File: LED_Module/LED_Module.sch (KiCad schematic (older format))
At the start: 16 parts, among them P3 CONN_02X04, P4 CONN_02X04, U1 AL8805WS, U2 AL8805WS

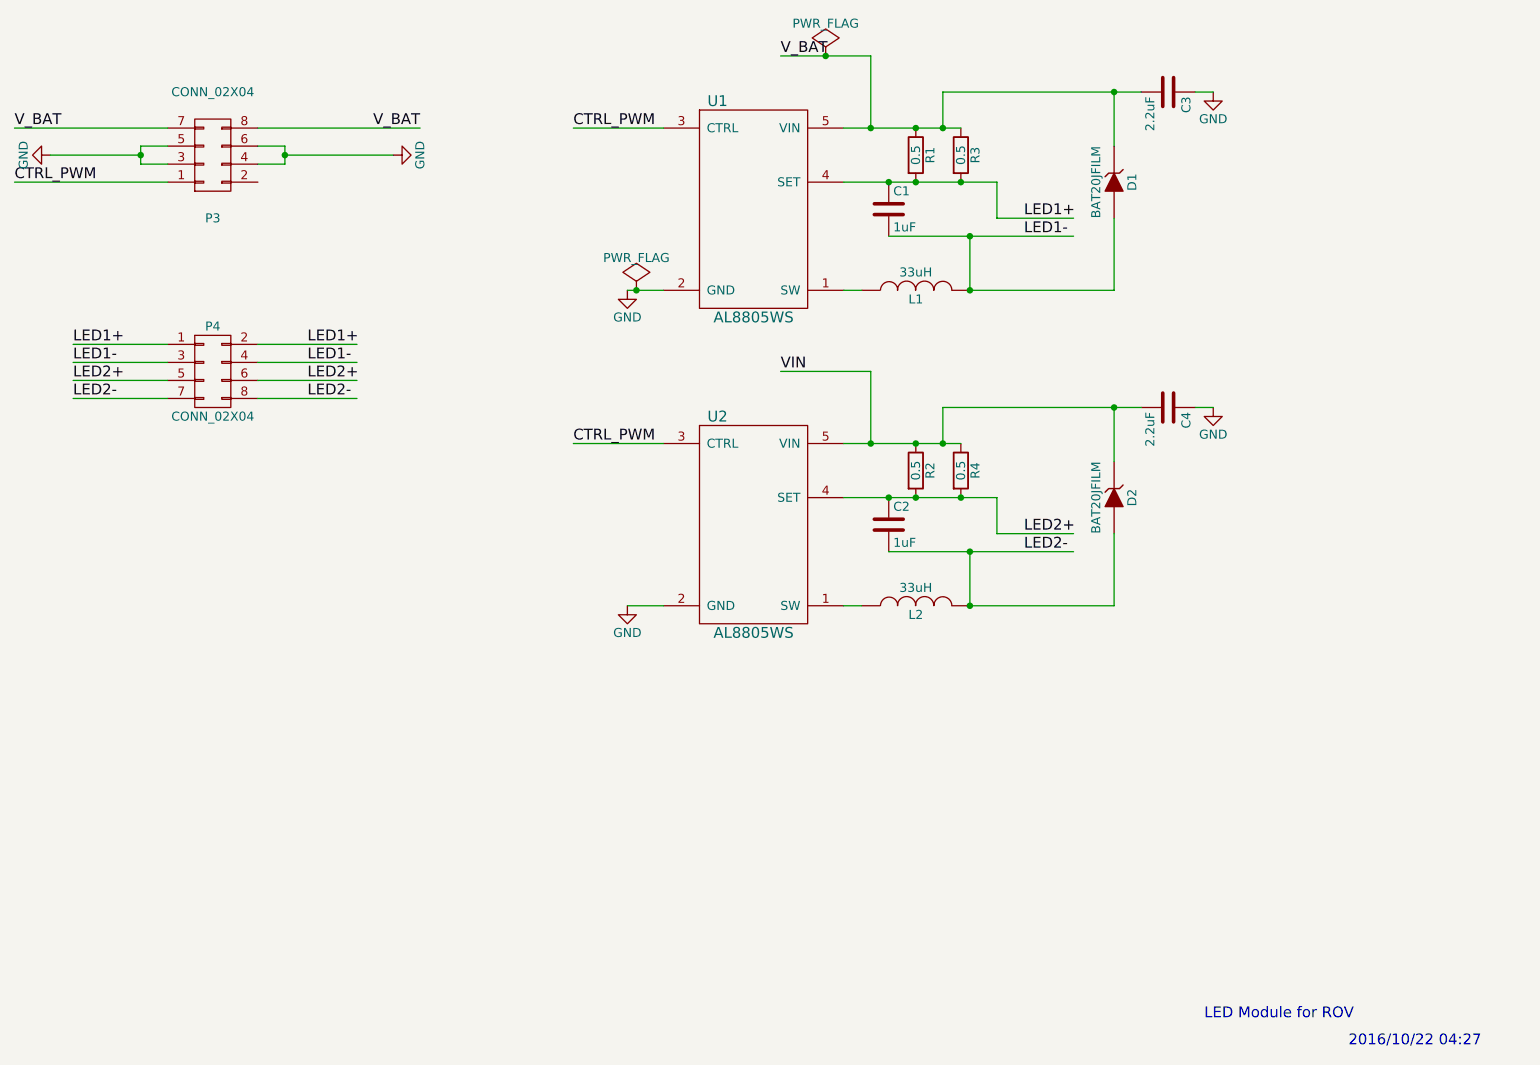
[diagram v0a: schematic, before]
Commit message: Recover LED_Module project
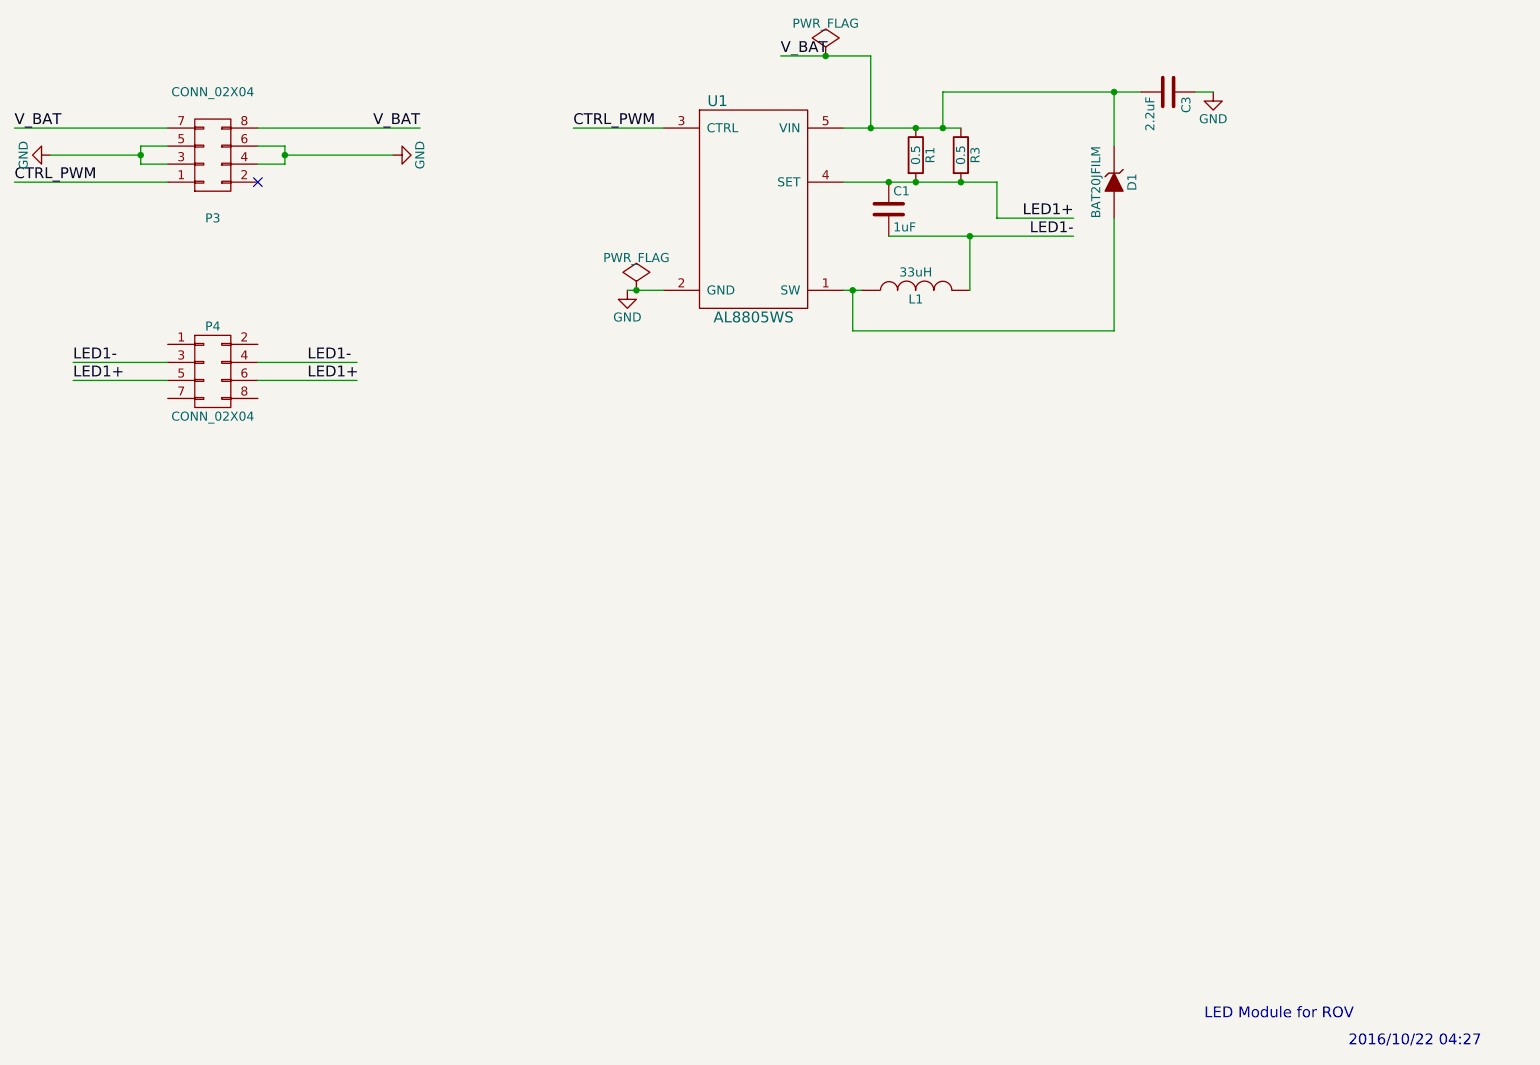
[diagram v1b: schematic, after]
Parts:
- removed C2: 1uF, Capacitors_SMD:C_0805_HandSoldering, symbol C
- removed C4: 2.2uF, Capacitors_SMD:C_0805_HandSoldering, symbol C
- removed D2: BAT20JFILM, w_smd_diode:sod323, symbol ZENER
- removed L2: 33uH, inductor:inductor_33uH, symbol INDUCTOR
- removed R2, R4: 0.5, Resistors_SMD:R_0805_HandSoldering, symbol R
- removed U2: AL8805WS, w_smd_trans:sot23-5, symbol AL8805WS
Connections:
- net labels removed: LED2+, LED2-, VIN
- wire segments 53 -> 33
- no-connect marks 0 -> 1
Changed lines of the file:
@@
 	1    0    0    -1
 $EndComp
-Wire Wire Line
-	5350 3450 5450 3450
-Wire Wire Line
-	5600 3150 6625 3150
-Wire Wire Line
-	6200 2850 6200 3050
-Connection ~ 5600 2850
 $Comp
 L R R1
@@
 	1    0    0    -1
 $EndComp
-Connection ~ 5750 2850
-Connection ~ 5750 2550
-Wire Wire Line
-	6050 3450 6050 3150
-Connection ~ 6050 3150
-Wire Wire Line
-	6050 3450 6850 3450
-Wire Wire Line
-	6850 3450 6850 3050
-Wire Wire Line
-	5900 2550 5900 2350
-Wire Wire Line
-	5900 2350 7000 2350
-Wire Wire Line
-	6850 2350 6850 2650
-Connection ~ 5900 2550
-Connection ~ 6850 2350
 $Comp
 L C C3
@@
 	1    0    0    -1
 $EndComp
-Wire Wire Line
-	7400 2350 7300 2350
-Wire Wire Line
-	5500 2150 5500 2550
-Wire Wire Line
-	5000 2150 5500 2150
-Connection ~ 5500 2550
-Wire Wire Line
-	3850 2550 4350 2550
 Text Label 3850 2550 0    60   ~ 0
 CTRL_PWM
@@
 V_BAT
 $Comp
-L AL8805WS U2
-U 1 1 580AA03A
-P 4850 4750
-F 0 "U2" H 4650 5350 60  0000 C CNN
-F 1 "AL8805WS" H 4850 4150 60  0000 C CNN
-F 2 "w_smd_trans:sot23-5" H 4850 4750 60  0001 C CNN
-F 3 "" H 4850 4750 60  0001 C CNN
-	1    4850 4750
-	1    0    0    -1
-$EndComp
-$Comp
-L INDUCTOR L2
-U 1 1 580AA040
-P 5750 5200
-F 0 "L2" V 5700 5200 50  0000 C CNN
-F 1 "33uH" V 5850 5200 50  0000 C CNN
-F 2 "inductor:inductor_33uH" H 5750 5200 50  0001 C CNN
-F 3 "" H 5750 5200 50  0000 C CNN
-	1    5750 5200
-	0    -1   -1   0
-$EndComp
-$Comp
-L GND #PWR03
-U 1 1 580AA058
-P 4150 5200
-F 0 "#PWR03" H 4150 4950 50  0001 C CNN
-F 1 "GND" H 4150 5050 50  0000 C CNN
-F 2 "" H 4150 5200 50  0000 C CNN
-F 3 "" H 4150 5200 50  0000 C CNN
-	1    4150 5200
-	1    0    0    -1
-$EndComp
-Wire Wire Line
-	4150 5200 4350 5200
-Wire Wire Line
-	5350 5200 5450 5200
-Wire Wire Line
-	5600 4900 6625 4900
-Wire Wire Line
-	6200 4600 6200 4800
-Wire Wire Line
-	6050 5200 6050 4900
-Connection ~ 6050 4900
-Wire Wire Line
-	6050 5200 6850 5200
-Wire Wire Line
-	6850 5200 6850 4800
-Wire Wire Line
-	5900 4300 5900 4100
-Wire Wire Line
-	5900 4100 7000 4100
-Wire Wire Line
-	6850 4100 6850 4400
-Connection ~ 5900 4300
-Connection ~ 6850 4100
-$Comp
-L C C4
-U 1 1 580AA079
-P 7150 4100
-F 0 "C4" H 7175 4200 50  0000 L CNN
-F 1 "2.2uF" H 7175 4000 50  0000 L CNN
-F 2 "Capacitors_SMD:C_0805_HandSoldering" H 7188 3950 50  0001 C CNN
-F 3 "" H 7150 4100 50  0000 C CNN
-	1    7150 4100
-	0    1    1    0
-$EndComp
-$Comp
-L GND #PWR04
-U 1 1 580AA07F
-P 7400 4100
-F 0 "#PWR04" H 7400 3850 50  0001 C CNN
-F 1 "GND" H 7400 3950 50  0000 C CNN
-F 2 "" H 7400 4100 50  0000 C CNN
-F 3 "" H 7400 4100 50  0000 C CNN
-	1    7400 4100
-	1    0    0    -1
-$EndComp
-Wire Wire Line
-	7400 4100 7300 4100
-Wire Wire Line
-	5500 4300 5500 3900
-Wire Wire Line
-	5500 3900 5000 3900
-Connection ~ 5500 4300
-Wire Wire Line
-	3850 4300 4350 4300
-Text Label 3850 4300 0    60   ~ 0
-CTRL_PWM
-Text Label 5000 3900 0    60   ~ 0
-VIN
-$Comp
-L PWR_FLAG #FLG05
+L PWR_FLAG #FLG03
 U 1 1 580AA3E5
 P 5250 2150
-F 0 "#FLG05" H 5250 2245 50  0001 C CNN
+F 0 "#FLG03" H 5250 2245 50  0001 C CNN
 F 1 "PWR_FLAG" H 5250 2330 50  0000 C CNN
 F 2 "" H 5250 2150 50  0000 C CNN
@@
 	1    0    0    -1
 $EndComp
-Connection ~ 5250 2150
-Wire Wire Line
-	4150 3450 4350 3450
-$Comp
-L PWR_FLAG #FLG06
+$Comp
+L PWR_FLAG #FLG04
 U 1 1 580AAE48
 P 4200 3450
-F 0 "#FLG06" H 4200 3545 50  0001 C CNN
+F 0 "#FLG04" H 4200 3545 50  0001 C CNN
 F 1 "PWR_FLAG" H 4200 3630 50  0000 C CNN
 F 2 "" H 4200 3450 50  0000 C CNN
@@
 	1    0    0    -1
 $EndComp
-Connection ~ 4200 3450
 Text Notes 7350 7500 0    60   ~ 0
 LED Module for ROV
@@
 	1    0    0    -1
 $EndComp
-Connection ~ 6000 2850
-$Comp
-L ZENER D2
-U 1 1 580C265A
-P 6850 4600
-F 0 "D2" H 6850 4700 50  0000 C CNN
-F 1 "BAT20JFILM" H 6850 4500 50  0000 C CNN
-F 2 "w_smd_diode:sod323" H 6850 4600 50  0001 C CNN
-F 3 "" H 6850 4600 50  0000 C CNN
-	1    6850 4600
-	0    1    1    0
-$EndComp
-Wire Wire Line
-	5350 4600 6200 4600
-Wire Wire Line
-	6000 4300 5350 4300
-Wire Wire Line
-	6200 2850 5350 2850
-Wire Wire Line
-	5350 2550 6000 2550
-$Comp
-L R R4
-U 1 1 580C75A6
-P 6000 4450
-F 0 "R4" V 6080 4450 50  0000 C CNN
-F 1 "0.5" V 6000 4450 50  0000 C CNN
-F 2 "Resistors_SMD:R_0805_HandSoldering" V 5930 4450 50  0001 C CNN
-F 3 "" H 6000 4450 50  0000 C CNN
-	1    6000 4450
-	1    0    0    -1
-$EndComp
-$Comp
-L R R2
-U 1 1 580C7673
-P 5750 4450
-F 0 "R2" V 5830 4450 50  0000 C CNN
-F 1 "0.5" V 5750 4450 50  0000 C CNN
-F 2 "Resistors_SMD:R_0805_HandSoldering" V 5680 4450 50  0001 C CNN
-F 3 "" H 5750 4450 50  0000 C CNN
-	1    5750 4450
-	1    0    0    -1
-$EndComp
-Connection ~ 6000 4600
-Connection ~ 5750 4600
-Connection ~ 5750 4300
 $Comp
 L INDUCTOR L1
@@
 	0    -1   -1   0
 $EndComp
-Connection ~ 6050 5200
-Connection ~ 6050 3450
-$Comp
-L C C2
-U 1 1 580CE3EF
-P 5600 4750
-F 0 "C2" H 5625 4850 50  0000 L CNN
-F 1 "1uF" H 5625 4650 50  0000 L CNN
-F 2 "Capacitors_SMD:C_0805_HandSoldering" H 5638 4600 50  0001 C CNN
-F 3 "" H 5600 4750 50  0000 C CNN
-	1    5600 4750
-	1    0    0    -1
-$EndComp
-Connection ~ 5600 4600
 $Comp
 L CONN_02X04 P3
@@
 	1    0    0    1
 $EndComp
-Wire Wire Line
-	1600 2850 750  2850
 Text Label 750  2850 0    60   ~ 0
 CTRL_PWM
-Wire Wire Line
-	1600 2550 750  2550
 Text Label 750  2550 0    60   ~ 0
 V_BAT
-Wire Wire Line
-	2100 2550 3000 2550
 Text Label 3000 2550 2    60   ~ 0
 V_BAT
-Wire Wire Line
-	2100 2650 2250 2650
-Wire Wire Line
-	2250 2650 2250 2750
-Wire Wire Line
-	2250 2750 2100 2750
-Wire Wire Line
-	1600 2650 1450 2650
-Wire Wire Line
-	1450 2650 1450 2750
-Wire Wire Line
-	1450 2750 1600 2750
-Wire Wire Line
-	2250 2700 2850 2700
-Connection ~ 2250 2700
-Wire Wire Line
-	1450 2700 950  2700
-Connection ~ 1450 2700
-$Comp
-L GND #PWR07
+$Comp
+L GND #PWR05
 U 1 1 580DCC21
 P 2850 2700
-F 0 "#PWR07" H 2850 2450 50  0001 C CNN
+F 0 "#PWR05" H 2850 2450 50  0001 C CNN
 F 1 "GND" H 2850 2550 50  0000 C CNN
 F 2 "" H 2850 2700 50  0000 C CNN
@@
 $EndComp
 $Comp
-L GND #PWR08
+L GND #PWR06
 U 1 1 580DCC57
 P 950 2700
-F 0 "#PWR08" H 950 2450 50  0001 C CNN
+F 0 "#PWR06" H 950 2450 50  0001 C CNN
 F 1 "GND" H 950 2550 50  0000 C CNN
 F 2 "" H 950 2700 50  0000 C CNN
@@
 	1    0    0    -1
 $EndComp
-Wire Wire Line
-	2100 3750 2650 3750
+Text Label 6625 3050 2    60   ~ 0
+LED1+
+Text Label 6625 3150 2    60   ~ 0
+LED1-
+Text Label 2375 3950 0    60   ~ 0
+LED1+
+Text Label 1075 3950 0    60   ~ 0
+LED1+
+Text Label 1075 3850 0    60   ~ 0
+LED1-
+Wire Wire Line
+	5350 3450 5450 3450
+Wire Wire Line
+	5600 3150 6625 3150
+Wire Wire Line
+	6200 2850 6200 3050
+Connection ~ 5600 2850
+Connection ~ 5750 2850
+Connection ~ 5750 2550
+Wire Wire Line
+	6050 3450 6050 3150
+Connection ~ 6050 3150
+Wire Wire Line
+	6850 3050 6850 3675
+Wire Wire Line
+	5900 2550 5900 2350
+Wire Wire Line
+	5900 2350 7000 2350
+Wire Wire Line
+	6850 2350 6850 2650
+Connection ~ 5900 2550
+Connection ~ 6850 2350
+Wire Wire Line
+	7400 2350 7300 2350
+Wire Wire Line
+	5500 2150 5500 2550
+Wire Wire Line
+	5000 2150 5500 2150
+Connection ~ 5500 2550
+Wire Wire Line
+	3850 2550 4350 2550
+Connection ~ 5250 2150
+Wire Wire Line
+	4150 3450 4350 3450
+Connection ~ 4200 3450
+Connection ~ 6000 2850
+Wire Wire Line
+	5350 2850 6200 2850
+Wire Wire Line
+	5350 2550 6000 2550
+Wire Wire Line
+	1600 2850 750  2850
+Wire Wire Line
+	1600 2550 750  2550
+Wire Wire Line
+	2100 2550 3000 2550
+Wire Wire Line
+	2100 2650 2250 2650
+Wire Wire Line
+	2250 2650 2250 2750
+Wire Wire Line
+	2250 2750 2100 2750
+Wire Wire Line
+	1600 2650 1450 2650
+Wire Wire Line
+	1450 2650 1450 2750
+Wire Wire Line
+	1450 2750 1600 2750
+Wire Wire Line
+	2250 2700 2850 2700
+Connection ~ 2250 2700
+Wire Wire Line
+	1450 2700 950  2700
+Connection ~ 1450 2700
 Wire Wire Line
 	2100 3850 2650 3850
@@
 	2100 3950 2650 3950
 Wire Wire Line
-	2100 4050 2650 4050
-Wire Wire Line
-	1600 3750 1075 3750
-Wire Wire Line
 	1600 3850 1075 3850
 Wire Wire Line
 	1600 3950 1075 3950
 Wire Wire Line
-	1600 4050 1075 4050
-Wire Wire Line
 	6200 3050 6625 3050
-Wire Wire Line
-	6200 4800 6625 4800
-Text Label 6350 3050 0    60   ~ 0
-LED1+
-Text Label 6350 3150 0    60   ~ 0
-LED1-
-Text Label 6350 4800 0    60   ~ 0
-LED2+
-Text Label 6350 4900 0    60   ~ 0
-LED2-
-Text Label 1075 3750 0    60   ~ 0
-LED1+
-Text Label 2375 3750 0    60   ~ 0
-LED1+
+NoConn ~ 2100 2850
+Wire Wire Line
+	5400 3450 5400 3675
+Wire Wire Line
+	5400 3675 6850 3675
+Connection ~ 5400 3450
 Text Label 2375 3850 0    60   ~ 0
 LED1-
-Text Label 1075 3850 0    60   ~ 0
-LED1-
-Text Label 1075 3950 0    60   ~ 0
-LED2+
-Text Label 2375 3950 0    60   ~ 0
-LED2+
-Text Label 2375 4050 0    60   ~ 0
-LED2-
-Text Label 1075 4050 0    60   ~ 0
-LED2-
 $EndSCHEMATC

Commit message: LED Modulization
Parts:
- removed P3, P4: CONN_02X04, KiCad_Footprint:Socket_Strip_Angled_2x04, symbol CONN_02X04
- added C2: C, Capacitors_SMD:c_elec_5x4.5, symbol C
- added D2: LED, KiCad_Footprint:Power_LED, symbol LED
- added P1: CONN_01X03, Connectors_JST:JST_XH_B03B-XH-A_03x2.50mm_Straight, symbol CONN_01X03
- added P2, P3: CONN_01X01, Wire_Pads:SolderWirePad_single_1-2mmDrill, symbol CONN_01X01
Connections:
- wire segments 33 -> 24
- no-connect marks 1 -> 0
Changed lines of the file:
@@
 L GND #PWR01
 U 1 1 580A7D6A
-P 4150 3450
-F 0 "#PWR01" H 4150 3200 50  0001 C CNN
-F 1 "GND" H 4150 3300 50  0000 C CNN
-F 2 "" H 4150 3450 50  0000 C CNN
-F 3 "" H 4150 3450 50  0000 C CNN
-	1    4150 3450
-	1    0    0    -1
+P 3950 3450
+F 0 "#PWR01" H 3950 3200 50  0001 C CNN
+F 1 "GND" H 3950 3300 50  0000 C CNN
+F 2 "" H 3950 3450 50  0000 C CNN
+F 3 "" H 3950 3450 50  0000 C CNN
+	1    3950 3450
+	0    1    1    0
 $EndComp
 $Comp
@@
 	0    -1   -1   0
 $EndComp
-$Comp
-L CONN_02X04 P3
-U 1 1 580D82DB
-P 1850 2700
-F 0 "P3" H 1850 3050 50  0000 C CNN
-F 1 "CONN_02X04" H 1850 2350 50  0000 C CNN
-F 2 "KiCad_Footprint:Socket_Strip_Angled_2x04" H 1850 1500 50  0001 C CNN
-F 3 "" H 1850 1500 50  0000 C CNN
-F 4 "DeviceMart" H 1850 2700 60  0001 C CNN "Vender"
-F 5 "5810" H 1850 2700 60  0001 C CNN "Part #"
-	1    1850 2700
-	1    0    0    1
-$EndComp
-Text Label 750  2850 0    60   ~ 0
-CTRL_PWM
-Text Label 750  2550 0    60   ~ 0
-V_BAT
-Text Label 3000 2550 2    60   ~ 0
-V_BAT
-$Comp
-L GND #PWR05
-U 1 1 580DCC21
-P 2850 2700
-F 0 "#PWR05" H 2850 2450 50  0001 C CNN
-F 1 "GND" H 2850 2550 50  0000 C CNN
-F 2 "" H 2850 2700 50  0000 C CNN
-F 3 "" H 2850 2700 50  0000 C CNN
-	1    2850 2700
-	0    -1   -1   0
-$EndComp
-$Comp
-L GND #PWR06
-U 1 1 580DCC57
-P 950 2700
-F 0 "#PWR06" H 950 2450 50  0001 C CNN
-F 1 "GND" H 950 2550 50  0000 C CNN
-F 2 "" H 950 2700 50  0000 C CNN
-F 3 "" H 950 2700 50  0000 C CNN
-	1    950  2700
-	0    1    1    0
-$EndComp
-$Comp
-L CONN_02X04 P4
-U 1 1 580C66C0
-P 1850 3900
-F 0 "P4" H 1850 4150 50  0000 C CNN
-F 1 "CONN_02X04" H 1850 3650 50  0000 C CNN
-F 2 "KiCad_Footprint:Socket_Strip_Angled_2x04" H 1850 2700 50  0001 C CNN
-F 3 "" H 1850 2700 50  0000 C CNN
-F 4 "DeviceMart" H 1850 3900 60  0001 C CNN "Vender"
-F 5 "5810" H 1850 3900 60  0001 C CNN "Part #"
-	1    1850 3900
-	1    0    0    -1
-$EndComp
-Text Label 6625 3050 2    60   ~ 0
+Text Label 6625 2850 2    60   ~ 0
 LED1+
 Text Label 6625 3150 2    60   ~ 0
 LED1-
-Text Label 2375 3950 0    60   ~ 0
-LED1+
-Text Label 1075 3950 0    60   ~ 0
-LED1+
-Text Label 1075 3850 0    60   ~ 0
-LED1-
 Wire Wire Line
 	5350 3450 5450 3450
 Wire Wire Line
 	5600 3150 6625 3150
-Wire Wire Line
-	6200 2850 6200 3050
 Connection ~ 5600 2850
 Connection ~ 5750 2850
@@
 Connection ~ 5250 2150
 Wire Wire Line
-	4150 3450 4350 3450
+	3950 3450 4350 3450
 Connection ~ 4200 3450
 Connection ~ 6000 2850
 Wire Wire Line
-	5350 2850 6200 2850
+	5350 2850 6625 2850
 Wire Wire Line
 	5350 2550 6000 2550
-Wire Wire Line
-	1600 2850 750  2850
-Wire Wire Line
-	1600 2550 750  2550
-Wire Wire Line
-	2100 2550 3000 2550
-Wire Wire Line
-	2100 2650 2250 2650
-Wire Wire Line
-	2250 2650 2250 2750
-Wire Wire Line
-	2250 2750 2100 2750
-Wire Wire Line
-	1600 2650 1450 2650
-Wire Wire Line
-	1450 2650 1450 2750
-Wire Wire Line
-	1450 2750 1600 2750
-Wire Wire Line
-	2250 2700 2850 2700
-Connection ~ 2250 2700
-Wire Wire Line
-	1450 2700 950  2700
-Connection ~ 1450 2700
-Wire Wire Line
-	2100 3850 2650 3850
-Wire Wire Line
-	2100 3950 2650 3950
-Wire Wire Line
-	1600 3850 1075 3850
-Wire Wire Line
-	1600 3950 1075 3950
-Wire Wire Line
-	6200 3050 6625 3050
-NoConn ~ 2100 2850
 Wire Wire Line
 	5400 3450 5400 3675
@@
 	5400 3675 6850 3675
 Connection ~ 5400 3450
-Text Label 2375 3850 0    60   ~ 0
+$Comp
+L CONN_01X03 P1
+U 1 1 58228E03
+P 4925 4675
+F 0 "P1" H 4925 4875 50  0000 C CNN
+F 1 "CONN_01X03" V 5025 4675 50  0000 C CNN
+F 2 "Connectors_JST:JST_XH_B03B-XH-A_03x2.50mm_Straight" H 4925 4675 50  0001 C CNN
+F 3 "" H 4925 4675 50  0000 C CNN
+	1    4925 4675
+	1    0    0    -1
+$EndComp
+Text Label 4050 4675 0    60   ~ 0
+V_BAT
+$Comp
+L GND #PWR05
+U 1 1 58229257
+P 4050 4575
+F 0 "#PWR05" H 4050 4325 50  0001 C CNN
+F 1 "GND" H 4050 4425 50  0000 C CNN
+F 2 "" H 4050 4575 50  0000 C CNN
+F 3 "" H 4050 4575 50  0000 C CNN
+	1    4050 4575
+	0    1    1    0
+$EndComp
+Wire Wire Line
+	4050 4675 4725 4675
+Text Label 4050 4775 0    60   ~ 0
+CTRL_PWM
+Wire Wire Line
+	4725 4775 4050 4775
+Wire Wire Line
+	4725 4575 4050 4575
+$Comp
+L LED D2
+U 1 1 582297B2
+P 6350 4625
+F 0 "D2" H 6350 4725 50  0000 C CNN
+F 1 "LED" H 6350 4525 50  0000 C CNN
+F 2 "KiCad_Footprint:Power_LED" H 6350 4800 50  0001 C CNN
+F 3 "" H 6350 4625 50  0000 C CNN
+	1    6350 4625
+	-1   0    0    1
+$EndComp
+Wire Wire Line
+	6150 4625 5600 4625
+Wire Wire Line
+	6550 4625 7150 4625
+Text Label 5900 4625 2    60   ~ 0
 LED1-
+Text Label 7150 4625 2    60   ~ 0
+LED1+
+$Comp
+L C C2
+U 1 1 5822AADF
+P 4625 5025
+F 0 "C2" H 4650 5125 50  0000 L CNN
+F 1 "C" H 4650 4925 50  0000 L CNN
+F 2 "Capacitors_SMD:c_elec_5x4.5" H 4663 4875 50  0001 C CNN
+F 3 "" H 4625 5025 50  0000 C CNN
+	1    4625 5025
+	1    0    0    -1
+$EndComp
+$Comp
+L GND #PWR06
+U 1 1 5822AB43
+P 4625 5175
+F 0 "#PWR06" H 4625 4925 50  0001 C CNN
+F 1 "GND" H 4625 5025 50  0000 C CNN
+F 2 "" H 4625 5175 50  0000 C CNN
+F 3 "" H 4625 5175 50  0000 C CNN
+	1    4625 5175
+	1    0    0    -1
+$EndComp
+Wire Wire Line
+	4625 4675 4625 4875
+Connection ~ 4625 4675
+$Comp
+L CONN_01X01 P2
+U 1 1 5822A57E
+P 5975 5175
+F 0 "P2" H 5975 5275 50  0000 C CNN
+F 1 "CONN_01X01" V 6075 5175 50  0000 C CNN
+F 2 "Wire_Pads:SolderWirePad_single_1-2mmDrill" H 5975 5175 50  0001 C CNN
+F 3 "" H 5975 5175 50  0000 C CNN
+	1    5975 5175
+	1    0    0    -1
+$EndComp
+$Comp
+L CONN_01X01 P3
+U 1 1 5822A779
+P 7000 5150
+F 0 "P3" H 7000 5250 50  0000 C CNN
+F 1 "CONN_01X01" V 7100 5150 50  0000 C CNN
+F 2 "Wire_Pads:SolderWirePad_single_1-2mmDrill" H 7000 5150 50  0001 C CNN
+F 3 "" H 7000 5150 50  0000 C CNN
+	1    7000 5150
+	1    0    0    -1
+$EndComp
+Text Label 5650 5175 2    60   ~ 0
+LED1+
+Text Label 6600 5150 2    60   ~ 0
+LED1-
+Wire Wire Line
+	5775 5175 5350 5175
+Wire Wire Line
+	6800 5150 6325 5150
 $EndSCHEMATC
